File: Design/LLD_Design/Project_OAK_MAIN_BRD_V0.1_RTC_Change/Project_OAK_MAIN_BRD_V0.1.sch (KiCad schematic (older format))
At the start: 112 parts, among them Q1 BC547, Q2 BC547, Q3 BC547, Q4 BC547, Q5 BC547, Q6 BC547, Q7 BC547, U1 ATmega328PB-MU, U2 RV-8263-C7-32.768KHZ-20PPM-TA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

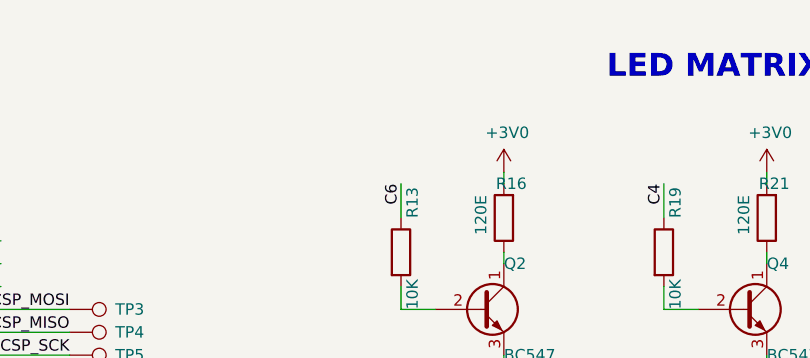
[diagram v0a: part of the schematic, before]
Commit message: Updated Blink code, SCH comments & added LED mapping details
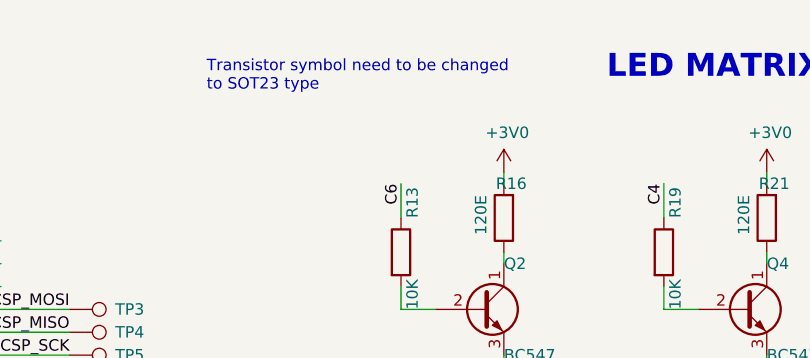
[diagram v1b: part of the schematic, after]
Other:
- note added: "Transistor symbol need to be changed\nto SOT23 type"
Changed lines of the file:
@@
 Text Notes 2050 5000 0    50   ~ 0
 connector signaling to be changed \nto 1&3 rather than 2&4
+Text Notes 6750 900  0    50   ~ 0
+Transistor symbol need to be changed\nto SOT23 type
 Text Notes 3900 5850 0    50   ~ 0
 connect CLKOE, CLKOUT to MCU pins.\nThis will be helpful in performing frequency compensation.
